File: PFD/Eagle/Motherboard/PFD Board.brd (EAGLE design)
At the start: 60 x 47 mm, 14 parts, among them IC1 MCP23017SO, SW1 1825910-6

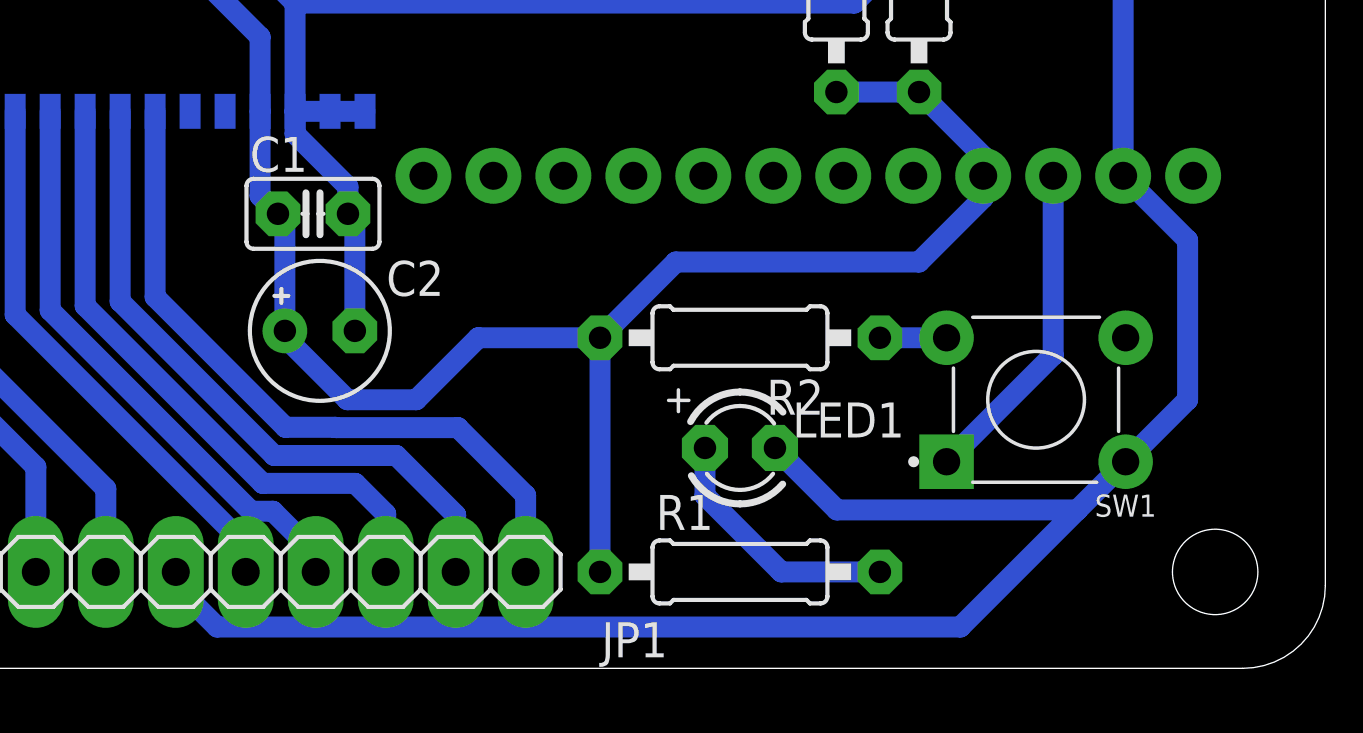
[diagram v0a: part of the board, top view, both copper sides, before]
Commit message: Corrected RESET switch design.
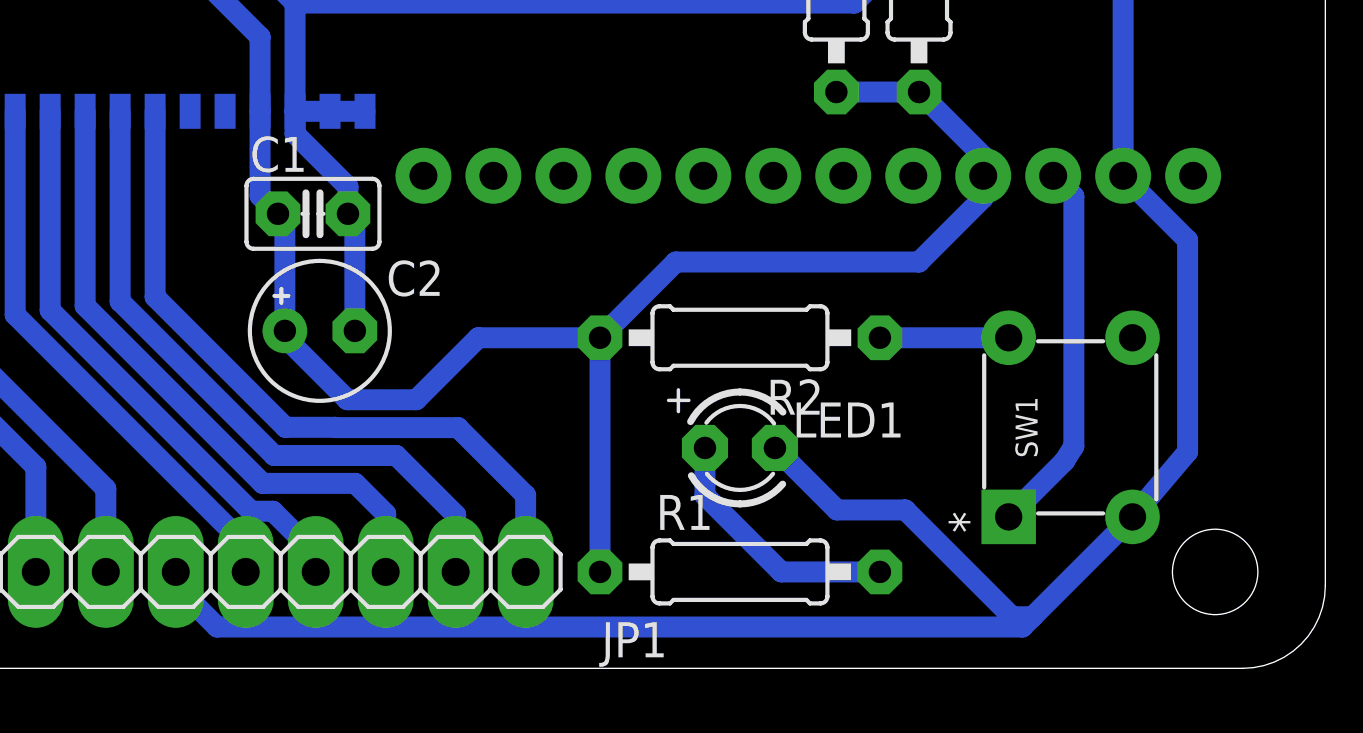
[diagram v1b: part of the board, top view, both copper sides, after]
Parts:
- SW1: value 1825910-6 -> 3-1825910-1; device Switch:1825910-6 -> Switches:SW4_1825910-H
- moved SW1 4.16 mm to (53.0, 12.0), turned to 90 degrees
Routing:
- net N$21: track 2.42 -> 4.67 mm
- net RESET: track 12.0 -> 13.6 mm
- net GND: track 132.6 -> 134.2 mm
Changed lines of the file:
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@@
 <attribute name="VALUE" x="44.615" y="28.2606" size="1.27" layer="27" ratio="10" rot="R270"/>
 </element>
-<element name="SW1" library="Switch" library_urn="urn:adsk.eagle:library:11396471" package="1825910-6" package3d_urn="urn:adsk.eagle:package:12788209/4" value="1825910-6" x="49.5" y="9.75" smashed="yes" rot="R180">
-<attribute name="CREATED_BY" value=" PCBLayout.com" x="31.72" y="64.36" size="1.778" layer="27" rot="R180" display="off"/>
-<attribute name="DIGIKEY_PART_NUMBER" value="450-1650-ND" x="31.72" y="64.36" size="1.778" layer="27" rot="R180" display="off"/>
-<attribute name="MANUFACTURER" value="TE Connectivity ALCOSWITCH Switches" x="31.72" y="64.36" size="1.778" layer="27" rot="R180" display="off"/>
-<attribute name="MPN" value="1825910-6" x="31.72" y="64.36" size="1.778" layer="27" rot="R180" display="off"/>
-<attribute name="NAME" x="53.864990625" y="6.306059375" size="0.800915625" layer="25" rot="R180"/>
-<attribute name="VALUE" x="53.95031875" y="14.110309375" size="0.80005625" layer="27" rot="R180"/>
+<element name="SW1" library="Switches" library_urn="urn:adsk.eagle:library:14854419" package="SW4_1825910-H" package3d_urn="urn:adsk.eagle:package:14854625/2" value="3-1825910-1" x="53" y="12" smashed="yes" rot="R90">
+<attribute name="BUILT_BY" value="EMA_UL_Team" x="53" y="12" size="1.778" layer="27" rot="R90" display="off"/>
+<attribute name="CATEGORY" value="Tactile Switches" x="53" y="12" size="1.778" layer="27" rot="R90" display="off"/>
+<attribute name="CONFIGURATION__POLE-THROW_" value="Single Pole - Single Throw" x="53" y="12" size="1.778" layer="27" rot="R90" display="off"/>
+<attribute name="COPYRIGHT" value="Copyright (C) 2016 Accelerated Designs. All rights reserved" x="53" y="12" size="1.778" layer="27" rot="R90" display="off"/>
+<attribute name="DESCRIPTION" value="FSM16JH=6MM TACT SWITCH, HIGH TEMP" x="53" y="12" size="1.778" layer="27" rot="R90" display="off"/>
+<attribute name="MANUFACTURER_PART_NUMBER" value="3-1825910-1" x="53" y="12" size="1.778" layer="27" rot="R90" display="off"/>
+<attribute name="MAX_SWITCHING_CURRENT" value="-" x="53" y="12" size="1.778" layer="27" rot="R90" display="off"/>
+<attribute name="MAX_SWITCHING_VOLTAGE_AC_" value="-" x="53" y="12" size="1.778" layer="27" rot="R90" display="off"/>
+<attribute name="NAME" x="49.556059375" y="7.635009375" size="0.800915625" layer="25" rot="R90"/>
+<attribute name="PART_STATUS" value="active" x="53" y="12" size="1.778" layer="27" rot="R90" display="off"/>
+<attribute name="PRODUCT_TYPE" value="Switch" x="53" y="12" size="1.778" layer="27" rot="R90" display="off"/>
+<attribute name="SERIES" value="Unknown" x="53" y="12" size="1.778" layer="27" rot="R90" display="off"/>
+<attribute name="SWITCH_TYPE" value="Tactile Switches" x="53" y="12" size="1.778" layer="27" rot="R90" display="off"/>
+<attribute name="TE_PART_NUMBER" value="3-1825910-1" x="53" y="12" size="1.778" layer="27" rot="R90" display="off"/>
+<attribute name="VALUE" x="57.360309375" y="7.54968125" size="0.80005625" layer="27" rot="R90"/>
+<attribute name="VENDOR" value="TE Connectivity" x="53" y="12" size="1.778" layer="27" rot="R90" display="off"/>
 </element>
 <element name="C1" library="rcl" library_urn="urn:adsk.eagle:library:334" package="C025-025X050" package3d_urn="urn:adsk.eagle:package:23629/2" value="" x="23.25" y="16.5" smashed="yes">
@@
 <wire x1="20.06" y1="26.69" x2="20.06" y2="29.78" width="0.762" layer="16"/>
 <wire x1="22.6" y1="24.15" x2="20.06" y2="26.69" width="0.762" layer="16"/>
-<wire x1="52.75" y1="7.5" x2="55" y2="9.75" width="0.762" layer="16"/>
+<wire x1="53" y1="5.4976" x2="55" y2="7.862109375" width="0.762" layer="16"/>
 <wire x1="55" y1="15.54" x2="52.66" y2="17.88" width="0.762" layer="16"/>
-<wire x1="55" y1="9.75" x2="55" y2="15.54" width="0.762" layer="16"/>
+<wire x1="55" y1="7.862109375" x2="55" y2="15.54" width="0.762" layer="16"/>
 <wire x1="52.66" y1="17.88" x2="52.66" y2="26.34" width="0.762" layer="16"/>
 <wire x1="52.66" y1="26.34" x2="50" y2="29" width="0.762" layer="16"/>
@@
 <wire x1="24.77" y1="16.25" x2="24.52" y2="16.5" width="0.762" layer="16"/>
 <wire x1="40.02" y1="8" x2="42.27" y2="5.75" width="0.762" layer="16"/>
-<wire x1="51" y1="5.75" x2="52.75" y2="7.5" width="0.762" layer="16"/>
-<wire x1="42.27" y1="5.75" x2="51" y2="5.75" width="0.762" layer="16"/>
+<wire x1="53.15129375" y1="5.75" x2="53" y2="5.4976" width="0.762" layer="16"/>
+<wire x1="42.27" y1="5.75" x2="44.75" y2="5.75" width="0.762" layer="16"/>
+<wire x1="53.15129375" y1="5.75" x2="53.25" y2="5.75" width="0.762" layer="16"/>
 <contactref element="JP1" pad="6"/>
 <wire x1="18.27" y1="3.5" x2="18.27" y2="3" width="0.762" layer="16"/>
-<wire x1="19.77" y1="1.5" x2="18.27" y2="3" width="0.762" layer="16"/>
-<wire x1="46.75" y1="1.5" x2="51" y2="5.75" width="0.762" layer="16"/>
-<wire x1="19.77" y1="1.5" x2="46.75" y2="1.5" width="0.762" layer="16"/>
+<wire x1="18.27" y1="3" x2="19.77" y2="1.5" width="0.762" layer="16"/>
+<wire x1="49.0024" y1="1.5" x2="49.3762" y2="1.8738" width="0.762" layer="16"/>
+<wire x1="49.3762" y1="1.8738" x2="53" y2="5.4976" width="0.762" layer="16"/>
+<wire x1="19.77" y1="1.5" x2="49.0024" y2="1.5" width="0.762" layer="16"/>
+<wire x1="48.6262" y1="1.8738" x2="49.3762" y2="1.8738" width="0.762" layer="16"/>
+<wire x1="44.75" y1="5.75" x2="48.6262" y2="1.8738" width="0.762" layer="16"/>
 </signal>
 <signal name="RESET">
 <contactref element="B1" pad="22"/>
 <contactref element="SW1" pad="1"/>
-<wire x1="46.25" y1="7.5" x2="50.12" y2="11.37" width="0.762" layer="16"/>
-<wire x1="50.12" y1="11.37" x2="50.12" y2="17.88" width="0.762" layer="16"/>
+<wire x1="50.87" y1="8.06301875" x2="50.53034375" y2="7.52374375" width="0.762" layer="16"/>
+<wire x1="48.5042" y1="5.4976" x2="50.53034375" y2="7.52374375" width="0.762" layer="16"/>
+<wire x1="50.87" y1="17.13" x2="50.12" y2="17.88" width="0.762" layer="16"/>
+<wire x1="50.87" y1="17.13" x2="50.87" y2="8.06301875" width="0.762" layer="16"/>
 </signal>
 <signal name="VCC">
@@
 <contactref element="R2" pad="1"/>
 <contactref element="SW1" pad="2"/>
-<wire x1="43.83" y1="12" x2="46.25" y2="12" width="0.762" layer="16"/>
+<wire x1="43.83" y1="12" x2="48.5042" y2="12" width="0.762" layer="16"/>
 </signal>
 <signal name="SDA">
